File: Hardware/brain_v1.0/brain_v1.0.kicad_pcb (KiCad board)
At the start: 2 copper layers, 100 x 100 mm, 83 parts, among them J1 Conn_01x02, J10 RFID, J11 Conn_01x05, J12 Conn_01x02, J13 Conn_01x02, J14 Conn_01x02, J15 Conn_01x04, J16 Conn_01x04, J2 Conn_01x02, J3 Conn_01x03, J4 JTAG, J5 Conn_01x02, J6 UART, J7 Conn_01x03, J8 UART Backup, J9 Conn_01x02, Q1 BSS138, Q2 BSS138, Q3 SMD-TRANSISTORS-NPN-25V-500MW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, Q4 SMD-TRANSISTORS-NPN-25V-500MW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, Q5 BSS138, Q6 BSS138, Q7 SMD-TRANSISTORS-NPN-25V-500MW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, SW1 SW_Push, SW2 SW_Push, U1 ESP32-WROOM-32E 4MB, U2 NAU7802SGI

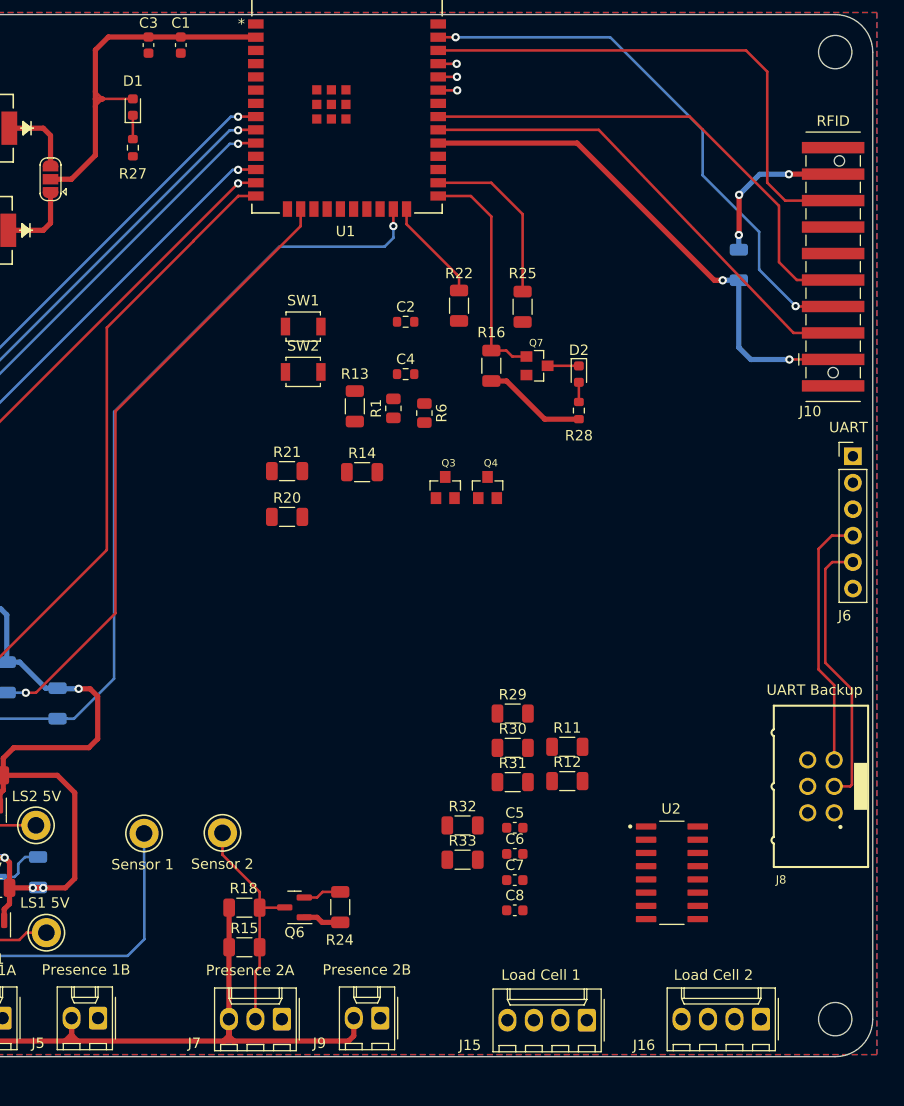
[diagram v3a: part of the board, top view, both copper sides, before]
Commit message: more than halfway done with brain, optimizing routing
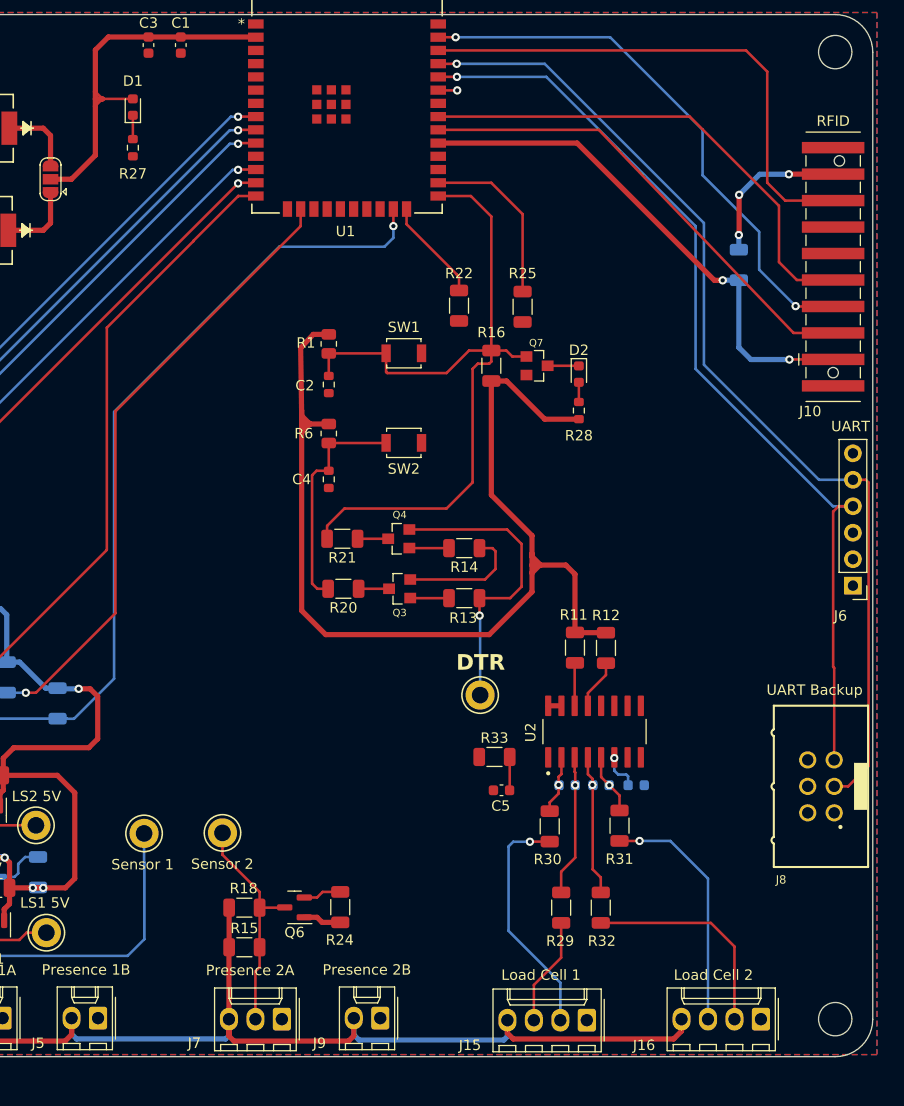
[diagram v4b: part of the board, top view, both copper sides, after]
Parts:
- added TP6: TestPoint, TestPoint:TestPoint_Keystone_5010-5014_Multipurpose, F.Cu at (163.9, 114.5)
- C6, C7, C8: moved to B.Cu
- moved R13 21.2 mm to (162.4, 105.2), turned to 180 degrees
- moved R29 19.2 mm to (171.7, 134.9), turned to 90 degrees
- moved C8 16.7 mm to (178.9, 123.2)
- moved U2 15.5 mm to (174.9, 118.0), turned to 90 degrees
- moved R32 15.4 mm to (175.5, 134.9), turned to 90 degrees
- moved R12 13.3 mm to (176.0, 110.0), turned to -90 degrees
- moved C4 12.5 mm to (149.4, 93.8), turned to -90 degrees
- moved J6 12.4 mm to (199.7, 104.0), turned to 180 degrees
- moved C7 12.3 mm to (175.5, 123.2), turned to 180 degrees
- moved R14 12.2 mm to (162.4, 100.4), turned to 180 degrees
- moved SW2 11.8 mm to (156.6, 90.3), turned to 180 degrees
- moved R31 11.1 mm to (177.3, 127.0), turned to 90 degrees
- moved Q3 10.7 mm to (156.2, 104.3), turned to 90 degrees
- moved R33 10.3 mm to (165.3, 120.4)
- moved SW1 9.99 mm to (156.6, 81.7), turned to 180 degrees
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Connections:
- J15 pad 4: +3V3 -> +5V
- J16 pad 4: +3V3 -> +5V
- J6 pad 6: unconnected-(J6-Pin_6-Pad6) -> /RTS
- R33 pad 1: +3V3 -> +5V
- U2 pad 15: +3V3 -> +5V
- U2 pad 16: +3V3 -> +5V
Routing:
- net +3V3: track 108.0 -> 204.0 mm
- net /TX_ESP: track 28.2 -> 97.2 mm
- net /RX_ESP: track 26.5 -> 90.9 mm
- net /GPIO0: track 22.4 -> 73.9 mm
- net +5V: track 129.9 -> 169.8 mm
- net /DTR: track 0.00 -> 29.3 mm, vias 0 -> 1
- net Net-(J16-Pin_3): track 0.00 -> 23.5 mm, vias 0 -> 1
- net Net-(J15-Pin_2): track 0.00 -> 22.9 mm, vias 0 -> 1
- net /CHIP_PU: track 0.00 -> 22.1 mm
- net Net-(J16-Pin_2): track 0.00 -> 20.7 mm
- net Net-(U2-VIN1P): track 0.00 -> 13.5 mm, vias 0 -> 1
- net Net-(U2-VIN2N): track 0.00 -> 13.5 mm, vias 0 -> 1
- net /RTS: track 0.00 -> 12.0 mm
- net Net-(J15-Pin_3): track 0.00 -> 10.4 mm
- net Net-(U2-VIN2P): track 0.00 -> 5.83 mm, vias 0 -> 1
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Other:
- board text added: "5V"
- board text added: "CTS"
- board text added: "DTR"
- board text added: "RTS"

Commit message: working on brain layout
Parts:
- moved R19 7.63 mm to (188.7, 80.8)
- moved U1 0.28 mm to (151.2, 55.1)
- moved C1 0.15 mm to (135.2, 52.3)
- moved C3 0.15 mm to (132.1, 52.3)
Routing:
- net /RTS: track 12.0 -> 55.4 mm, vias 0 -> 2
- net +3V3: track 204.0 -> 241.1 mm, vias 8 -> 9
- net /RFID_CS: track 50.4 -> 51.3 mm

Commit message: brain done! except for stitching vias
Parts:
- moved J12 34.6 mm to (105.3, 116.9)
- moved J11 10.5 mm to (103.6, 90.4)
- moved J4 10.3 mm to (103.6, 98.9)
- moved R10 10.3 mm to (118.6, 102.5)
- moved R26 10.3 mm to (114.0, 100.0)
- moved R5 10.3 mm to (109.6, 97.5)
- moved R9 10.3 mm to (123.5, 105.0)
- moved TP2 1.95 mm to (121.6, 125.1)
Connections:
- J11 pad 1: /GPIO21 -> /GPIO27
- J11 pad 2: /GPIO27 -> /GPIO26
- U1 pad 11: /ADC_DRDY -> /GPIO26
- U1 pad 33: /GPIO21 -> /ADC_DRDY
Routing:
- net /CHIP_PU: track 22.1 -> 156.7 mm, vias 0 -> 5
- net /GPIO0: track 74.0 -> 169.1 mm, vias 0 -> 1
- net /Sensor2: track 3.67 -> 92.8 mm, vias 0 -> 2
- net /Sensor1: track 5.04 -> 91.1 mm, vias 0 -> 1
- net +3V3: track 241.1 -> 319.9 mm, vias 9 -> 36
- net /ADC_DRDY: track 0.00 -> 77.3 mm, vias 0 -> 2
- net /ADC_SDA: track 4.13 -> 77.1 mm, vias 0 -> 2
- net /ADC_SCL: track 4.81 -> 70.5 mm, vias 0 -> 2
- net /GPIO26: track 0.00 -> 49.3 mm
- net /TDO: track 89.3 -> 73.1 mm
- net /TCK: track 75.0 -> 64.2 mm
- net /TDI: track 70.1 -> 59.6 mm
- net /TMS: track 66.0 -> 55.6 mm, vias 2 -> 1
- net /GPIO25: track 54.1 -> 48.8 mm, vias 2 -> 0
- net /GPIO33: track 52.7 -> 48.3 mm, vias 2 -> 0
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- added copper zone on B.Cu, net +3V3
- added copper zone on F.Cu, net +3V3
- added copper zone on B.Cu, net /MCU_Power
- added copper zone on F.Cu, net /MCU_Power

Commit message: done with brain v1
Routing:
- net +3V3: track 319.9 -> 343.3 mm, vias 36 -> 40
- net +5V: track 170.9 -> 188.9 mm, vias 0 -> 8
- net GND: vias 0 -> 184
- added copper zone on B.Cu, net +5V
- added copper zone on F.Cu, net +5V
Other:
- board text added: "JTAG"
- board text removed: "JTAG/Motor Driver IN"
